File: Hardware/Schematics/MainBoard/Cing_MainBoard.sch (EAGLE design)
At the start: 178 parts, among them IC1 L293D, IC2 LM2576S, IC3 FT232RL, IC5 BME280, Q1 16mhz, Q2 BSS138, Q3 BSS138, Q4 BSS138, Q5 BSS138, Q6 NP2301AMR-G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

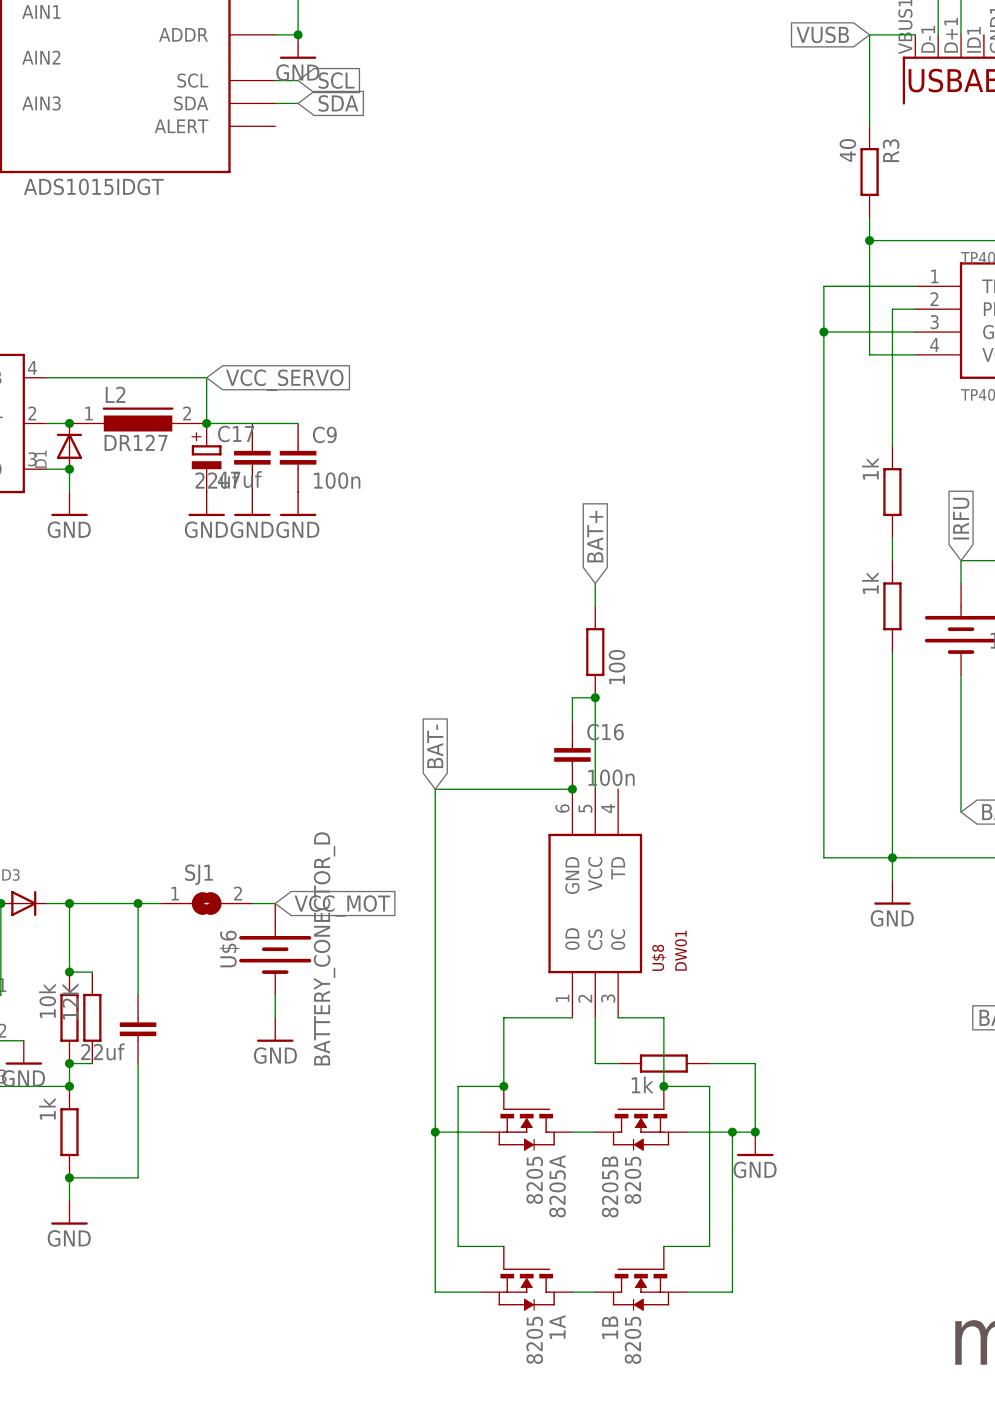
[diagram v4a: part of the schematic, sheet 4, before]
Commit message: adding more protection (motor fix)
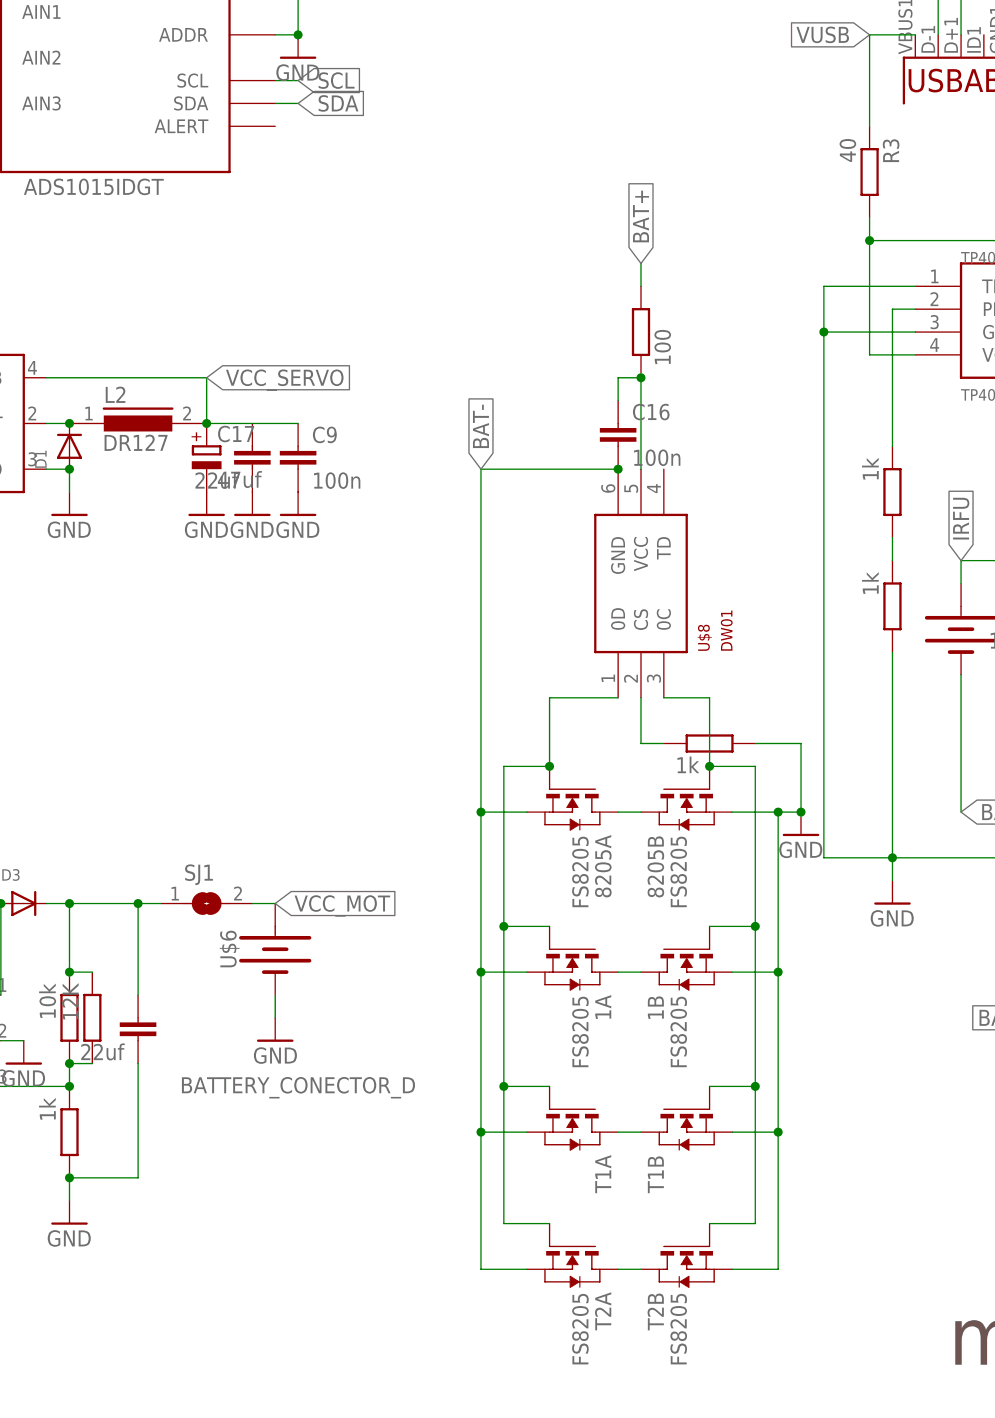
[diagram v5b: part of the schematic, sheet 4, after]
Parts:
- added T1, T2: FS8205, FS8205A:DMN3024LSD
- 1, 8205: value 8205 -> FS8205
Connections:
- new net N$67: T1A.D, T1B.D
- new net N$68: T2A.D, T2B.D
- net BAT-: now also T1A.S, T2A.S
- net GND: now also T1B.S, T2B.S
- net N$48: now also T1A.G, T2A.G
- net N$49: now also T1B.G, T2B.G
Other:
- moved on the sheet: 1A, 1B, 8205A, 8205B, C16, U$8

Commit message: adding CH330N
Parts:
- added C28, C29: 100n, rcl:C-EUC1206
- added U4: CH330N, Cing Library:CH330N
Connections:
- net +3V3: now also C28.1, C29.2, U4.V3, U4.VCC
- net D+: now also U4.USB_D+
- net D-: now also U4.USB_D-
- net GND: now also C28.2, C29.1, U1.USBID, U4.GND
- net RXD: now also U4.TXD
- net TXD: now also U4.RXD
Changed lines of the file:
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@@
 <part name="T1" library="FS8205A" deviceset="DMN3024LSD" device="" value="FS8205"/>
 <part name="T2" library="FS8205A" deviceset="DMN3024LSD" device="" value="FS8205"/>
+<part name="U4" library="Cing Library" library_urn="urn:adsk.eagle:library:10154637" deviceset="CH330N" device="" package3d_urn="urn:adsk.eagle:package:10906029/3"/>
+<part name="GND49" library="supply1" library_urn="urn:adsk.eagle:library:371" deviceset="GND" device=""/>
+<part name="C28" library="rcl" library_urn="urn:adsk.eagle:library:334" deviceset="C-EU" device="C1206" package3d_urn="urn:adsk.eagle:package:23618/2" value="100n"/>
+<part name="C29" library="rcl" library_urn="urn:adsk.eagle:library:334" deviceset="C-EU" device="C1206" package3d_urn="urn:adsk.eagle:package:23618/2" value="100n"/>
+<part name="GND61" library="supply1" library_urn="urn:adsk.eagle:library:371" deviceset="GND" device=""/>
+<part name="GND65" library="supply1" library_urn="urn:adsk.eagle:library:371" deviceset="GND" device=""/>
+<part name="+3V13" library="supply1" library_urn="urn:adsk.eagle:library:371" deviceset="+3V3" device=""/>
 </parts>
 <sheets>
@@
 <wire x1="175.26" y1="152.4" x2="170.18" y2="152.4" width="0.1524" layer="91"/>
 <pinref part="U1" gate="G$1" pin="GND"/>
+<pinref part="U1" gate="G$1" pin="USBID"/>
+<wire x1="170.18" y1="152.4" x2="167.64" y2="152.4" width="0.1524" layer="91"/>
+<junction x="170.18" y="152.4"/>
 </segment>
 <segment>
@@
 <attribute name="VALUE" x="200.66" y="132.08" size="1.778" layer="96"/>
 </instance>
-<instance part="R30" gate="G$1" x="175.26" y="83.82" smashed="yes" rot="MR90">
-<attribute name="VALUE" x="171.958" y="80.01" size="1.778" layer="96" rot="MR90"/>
-</instance>
-<instance part="R31" gate="G$1" x="180.34" y="83.82" smashed="yes" rot="MR90">
-<attribute name="VALUE" x="177.038" y="80.01" size="1.778" layer="96" rot="MR90"/>
-</instance>
-<instance part="+3V3" gate="G$1" x="177.8" y="99.06" smashed="yes">
-<attribute name="VALUE" x="175.26" y="93.98" size="1.778" layer="96" rot="R90"/>
+<instance part="R30" gate="G$1" x="187.96" y="106.68" smashed="yes" rot="MR90">
+<attribute name="VALUE" x="184.658" y="102.87" size="1.778" layer="96" rot="MR90"/>
+</instance>
+<instance part="R31" gate="G$1" x="193.04" y="106.68" smashed="yes" rot="MR90">
+<attribute name="VALUE" x="189.738" y="102.87" size="1.778" layer="96" rot="MR90"/>
+</instance>
+<instance part="+3V3" gate="G$1" x="190.5" y="121.92" smashed="yes">
+<attribute name="VALUE" x="187.96" y="116.84" size="1.778" layer="96" rot="R90"/>
 </instance>
 <instance part="+3V5" gate="G$1" x="210.82" y="152.4" smashed="yes">
@@
 <instance part="C22" gate="G$1" x="198.12" y="142.24" smashed="yes">
 <attribute name="VALUE" x="194.564" y="142.621" size="1.778" layer="96"/>
+</instance>
+<instance part="U4" gate="G$1" x="170.18" y="48.26" smashed="yes">
+<attribute name="NAME" x="175.26" y="58.42" size="2.1844" layer="95"/>
+<attribute name="VALUE" x="175.26" y="35.56" size="2.1844" layer="96"/>
+</instance>
+<instance part="GND49" gate="1" x="172.72" y="27.94" smashed="yes" rot="MR0">
+<attribute name="VALUE" x="175.26" y="25.4" size="1.778" layer="96" rot="MR0"/>
+</instance>
+<instance part="C28" gate="G$1" x="177.8" y="66.04" smashed="yes" rot="R90">
+<attribute name="NAME" x="177.419" y="67.564" size="1.778" layer="95" rot="R90"/>
+<attribute name="VALUE" x="182.499" y="67.564" size="1.778" layer="96" rot="R90"/>
+</instance>
+<instance part="C29" gate="G$1" x="165.1" y="66.04" smashed="yes" rot="R90">
+<attribute name="NAME" x="164.719" y="67.564" size="1.778" layer="95" rot="R90"/>
+<attribute name="VALUE" x="169.799" y="67.564" size="1.778" layer="96" rot="R90"/>
+</instance>
+<instance part="GND61" gate="1" x="182.88" y="60.96" smashed="yes" rot="MR0">
+<attribute name="VALUE" x="185.42" y="58.42" size="1.778" layer="96" rot="MR0"/>
+</instance>
+<instance part="GND65" gate="1" x="162.56" y="60.96" smashed="yes" rot="MR0">
+<attribute name="VALUE" x="165.1" y="58.42" size="1.778" layer="96" rot="MR0"/>
+</instance>
+<instance part="+3V13" gate="G$1" x="172.72" y="81.28" smashed="yes">
+<attribute name="VALUE" x="170.18" y="76.2" size="1.778" layer="96" rot="R90"/>
 </instance>
 </instances>
@@
 <pinref part="GND58" gate="1" pin="GND"/>
 </segment>
+<segment>
+<pinref part="U4" gate="G$1" pin="GND"/>
+<pinref part="GND49" gate="1" pin="GND"/>
+<wire x1="172.72" y1="30.48" x2="172.72" y2="33.02" width="0.1524" layer="91"/>
+</segment>
+<segment>
+<pinref part="C28" gate="G$1" pin="2"/>
+<pinref part="GND61" gate="1" pin="GND"/>
+<wire x1="182.88" y1="66.04" x2="182.88" y2="63.5" width="0.1524" layer="91"/>
+</segment>
+<segment>
+<pinref part="C29" gate="G$1" pin="1"/>
+<pinref part="GND65" gate="1" pin="GND"/>
+<wire x1="162.56" y1="66.04" x2="162.56" y2="63.5" width="0.1524" layer="91"/>
+</segment>
 </net>
 <net name="N$20" class="0">
@@
 <pinref part="IC3" gate="G$1" pin="USBDM"/>
 </segment>
+<segment>
+<pinref part="U4" gate="G$1" pin="USB_D-"/>
+<wire x1="190.5" y1="48.26" x2="193.04" y2="48.26" width="0.1524" layer="91"/>
+<label x="193.04" y="48.26" size="1.778" layer="95" xref="yes"/>
+</segment>
 </net>
 <net name="D+" class="0">
@@
 <label x="106.68" y="137.16" size="1.778" layer="95" rot="R180" xref="yes"/>
 <pinref part="IC3" gate="G$1" pin="USBDP"/>
+</segment>
+<segment>
+<pinref part="U4" gate="G$1" pin="USB_D+"/>
+<wire x1="190.5" y1="43.18" x2="193.04" y2="43.18" width="0.1524" layer="91"/>
+<label x="193.04" y="43.18" size="1.778" layer="95" xref="yes"/>
 </segment>
 </net>
@@
 <wire x1="157.48" y1="154.94" x2="157.48" y2="144.78" width="0.1524" layer="91"/>
 </segment>
+<segment>
+<pinref part="U4" gate="G$1" pin="RXD"/>
+<wire x1="154.94" y1="53.34" x2="152.4" y2="53.34" width="0.1524" layer="91"/>
+<label x="152.4" y="53.34" size="1.778" layer="95" rot="R180" xref="yes"/>
+</segment>
 </net>
 <net name="RXD" class="0">
@@
 <wire x1="152.4" y1="154.94" x2="152.4" y2="147.32" width="0.1524" layer="91"/>
 </segment>
+<segment>
+<pinref part="U4" gate="G$1" pin="TXD"/>
+<wire x1="154.94" y1="43.18" x2="152.4" y2="43.18" width="0.1524" layer="91"/>
+<label x="152.4" y="43.18" size="1.778" layer="95" rot="R180" xref="yes"/>
+</segment>
 </net>
 <net name="SCL" class="0">
@@
 <segment>
 <pinref part="R30" gate="G$1" pin="1"/>
-<wire x1="175.26" y1="78.74" x2="170.18" y2="78.74" width="0.1524" layer="91"/>
-<label x="170.18" y="78.74" size="1.778" layer="95" rot="R180" xref="yes"/>
+<wire x1="187.96" y1="101.6" x2="182.88" y2="101.6" width="0.1524" layer="91"/>
+<label x="182.88" y="101.6" size="1.778" layer="95" rot="R180" xref="yes"/>
 </segment>
 <segment>
@@
 <segment>
 <pinref part="R31" gate="G$1" pin="1"/>
-<wire x1="180.34" y1="78.74" x2="182.88" y2="78.74" width="0.1524" layer="91"/>
-<label x="182.88" y="78.74" size="1.778" layer="95" xref="yes"/>
+<wire x1="193.04" y1="101.6" x2="195.58" y2="101.6" width="0.1524" layer="91"/>
+<label x="195.58" y="101.6" size="1.778" layer="95" xref="yes"/>
 </segment>
 <segment>
@@
 <pinref part="R30" gate="G$1" pin="2"/>
 <pinref part="R31" gate="G$1" pin="2"/>
-<wire x1="180.34" y1="88.9" x2="177.8" y2="88.9" width="0.1524" layer="91"/>
+<wire x1="193.04" y1="111.76" x2="190.5" y2="111.76" width="0.1524" layer="91"/>
 <pinref part="+3V3" gate="G$1" pin="+3V3"/>
-<wire x1="177.8" y1="96.52" x2="177.8" y2="88.9" width="0.1524" layer="91"/>
-<junction x="177.8" y="88.9"/>
-<wire x1="177.8" y1="88.9" x2="175.26" y2="88.9" width="0.1524" layer="91"/>
+<wire x1="190.5" y1="119.38" x2="190.5" y2="111.76" width="0.1524" layer="91"/>
+<junction x="190.5" y="111.76"/>
+<wire x1="190.5" y1="111.76" x2="187.96" y2="111.76" width="0.1524" layer="91"/>
 </segment>
 <segment>
@@
 <pinref part="+3V38" gate="G$1" pin="+3V3"/>
 </segment>
-</net>
+<segment>
+<pinref part="U4" gate="G$1" pin="VCC"/>
+<pinref part="C28" gate="G$1" pin="1"/>
+<wire x1="175.26" y1="66.04" x2="175.26" y2="63.5" width="0.1524" layer="91"/>
+<pinref part="U4" gate="G$1" pin="V3"/>
+<pinref part="C29" gate="G$1" pin="2"/>
+<wire x1="170.18" y1="66.04" x2="170.18" y2="63.5" width="0.1524" layer="91"/>
+<wire x1="175.26" y1="66.04" x2="172.72" y2="66.04" width="0.1524" layer="91"/>
+<junction x="175.26" y="66.04"/>
+<junction x="170.18" y="66.04"/>
+<pinref part="+3V13" gate="G$1" pin="+3V3"/>
+<wire x1="172.72" y1="66.04" x2="170.18" y2="66.04" width="0.1524" layer="91"/>
+<wire x1="172.72" y1="66.04" x2="172.72" y2="78.74" width="0.1524" layer="91"/>
+<junction x="172.72" y="66.04"/>
+</segment>
+</net>

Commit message: commit
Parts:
- added C30, C31: 100n, rcl:C-EUC1206
- added IC4: BMP280, bosch-bmp280:BMP280
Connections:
- net +3V3: now also C30.2, C31.2, IC4.CSB, IC4.SDO, IC4.VDD, IC4.VDDIO
- net GND: now also C30.1, C31.1, IC4.GND
- net SCL: now also IC4.SCK
- net SDA: now also IC4.SDI
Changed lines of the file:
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@@
 <part name="GND65" library="supply1" library_urn="urn:adsk.eagle:library:371" deviceset="GND" device=""/>
 <part name="+3V13" library="supply1" library_urn="urn:adsk.eagle:library:371" deviceset="+3V3" device=""/>
+<part name="FRAME7" library="frames" library_urn="urn:adsk.eagle:library:229" deviceset="A4L-LOC" device=""/>
+<part name="IC4" library="bosch-bmp280" deviceset="BMP280" device=""/>
+<part name="+3V14" library="supply1" library_urn="urn:adsk.eagle:library:371" deviceset="+3V3" device=""/>
+<part name="+3V15" library="supply1" library_urn="urn:adsk.eagle:library:371" deviceset="+3V3" device=""/>
+<part name="GND71" library="supply1" library_urn="urn:adsk.eagle:library:371" deviceset="GND" device=""/>
+<part name="+3V16" library="supply1" library_urn="urn:adsk.eagle:library:371" deviceset="+3V3" device=""/>
+<part name="+3V19" library="supply1" library_urn="urn:adsk.eagle:library:371" deviceset="+3V3" device=""/>
+<part name="C30" library="rcl" library_urn="urn:adsk.eagle:library:334" deviceset="C-EU" device="C1206" package3d_urn="urn:adsk.eagle:package:23618/2" value="100n"/>
+<part name="+3V24" library="supply1" library_urn="urn:adsk.eagle:library:371" deviceset="+3V3" device=""/>
+<part name="GND72" library="supply1" library_urn="urn:adsk.eagle:library:371" deviceset="GND" device=""/>
+<part name="C31" library="rcl" library_urn="urn:adsk.eagle:library:334" deviceset="C-EU" device="C1206" package3d_urn="urn:adsk.eagle:package:23618/2" value="100n"/>
+<part name="+3V25" library="supply1" library_urn="urn:adsk.eagle:library:371" deviceset="+3V3" device=""/>
+<part name="GND73" library="supply1" library_urn="urn:adsk.eagle:library:371" deviceset="GND" device=""/>
 </parts>
 <sheets>
@@
 <attribute name="VALUE" x="170.18" y="76.2" size="1.778" layer="96" rot="R90"/>
 </instance>
+<instance part="IC4" gate="G$1" x="223.52" y="40.64" smashed="yes">
+<attribute name="NAME" x="213.614" y="49.022" size="1.778" layer="95" font="vector"/>
+<attribute name="VALUE" x="213.36" y="30.48" size="1.778" layer="96" font="vector"/>
+</instance>
+<instance part="+3V14" gate="G$1" x="208.28" y="48.26" smashed="yes">
+<attribute name="VALUE" x="208.28" y="48.26" size="1.778" layer="96" rot="R90"/>
+</instance>
+<instance part="+3V15" gate="G$1" x="238.76" y="48.26" smashed="yes">
+<attribute name="VALUE" x="236.22" y="43.18" size="1.778" layer="96" rot="R90"/>
+</instance>
+<instance part="GND71" gate="1" x="208.28" y="33.02" smashed="yes" rot="MR0">
+<attribute name="VALUE" x="210.82" y="30.48" size="1.778" layer="96" rot="MR0"/>
+</instance>
+<instance part="+3V16" gate="G$1" x="208.28" y="43.18" smashed="yes">
+<attribute name="VALUE" x="208.28" y="43.18" size="1.778" layer="96" rot="R90"/>
+</instance>
+<instance part="+3V19" gate="G$1" x="241.3" y="35.56" smashed="yes" rot="R270">
+<attribute name="VALUE" x="241.3" y="33.02" size="1.778" layer="96"/>
+</instance>
+<instance part="C30" gate="G$1" x="243.84" y="53.34" smashed="yes" rot="R180">
+<attribute name="NAME" x="242.316" y="52.959" size="1.778" layer="95" rot="R180"/>
+<attribute name="VALUE" x="242.316" y="58.039" size="1.778" layer="96" rot="R180"/>
+</instance>
+<instance part="+3V24" gate="G$1" x="243.84" y="60.96" smashed="yes">
+<attribute name="VALUE" x="241.3" y="55.88" size="1.778" layer="96" rot="R90"/>
+</instance>
+<instance part="GND72" gate="1" x="243.84" y="48.26" smashed="yes" rot="MR0">
+<attribute name="VALUE" x="246.38" y="45.72" size="1.778" layer="96" rot="MR0"/>
+</instance>
+<instance part="C31" gate="G$1" x="251.46" y="53.34" smashed="yes" rot="R180">
+<attribute name="NAME" x="249.936" y="52.959" size="1.778" layer="95" rot="R180"/>
+<attribute name="VALUE" x="249.936" y="58.039" size="1.778" layer="96" rot="R180"/>
+</instance>
+<instance part="+3V25" gate="G$1" x="251.46" y="60.96" smashed="yes">
+<attribute name="VALUE" x="248.92" y="55.88" size="1.778" layer="96" rot="R90"/>
+</instance>
+<instance part="GND73" gate="1" x="251.46" y="48.26" smashed="yes" rot="MR0">
+<attribute name="VALUE" x="254" y="45.72" size="1.778" layer="96" rot="MR0"/>
+</instance>
 </instances>
 <busses>
@@
 <wire x1="162.56" y1="66.04" x2="162.56" y2="63.5" width="0.1524" layer="91"/>
 </segment>
+<segment>
+<pinref part="IC4" gate="G$1" pin="GND"/>
+<pinref part="GND71" gate="1" pin="GND"/>
+</segment>
+<segment>
+<pinref part="C30" gate="G$1" pin="1"/>
+<pinref part="GND72" gate="1" pin="GND"/>
+</segment>
+<segment>
+<pinref part="C31" gate="G$1" pin="1"/>
+<pinref part="GND73" gate="1" pin="GND"/>
+</segment>
 </net>
 <net name="N$20" class="0">
@@
 <label x="231.14" y="68.58" size="1.778" layer="95" xref="yes"/>
 </segment>
+<segment>
+<pinref part="IC4" gate="G$1" pin="SCK"/>
+<wire x1="238.76" y1="40.64" x2="241.3" y2="40.64" width="0.1524" layer="91"/>
+<label x="241.3" y="40.64" size="1.778" layer="95" xref="yes"/>
+</segment>
 </net>
 <net name="SDA" class="0">
@@
 <label x="231.14" y="66.04" size="1.778" layer="95" xref="yes"/>
 </segment>
+<segment>
+<pinref part="IC4" gate="G$1" pin="SDI"/>
+<wire x1="238.76" y1="38.1" x2="241.3" y2="38.1" width="0.1524" layer="91"/>
+<label x="241.3" y="38.1" size="1.778" layer="95" xref="yes"/>
+</segment>
 </net>
 <net name="+3V3" class="0">
@@
 <junction x="172.72" y="66.04"/>
 </segment>
+<segment>
+<pinref part="IC4" gate="G$1" pin="VDD"/>
+<pinref part="+3V14" gate="G$1" pin="+3V3"/>
+</segment>
+<segment>
+<pinref part="IC4" gate="G$1" pin="VDDIO"/>
+<pinref part="+3V15" gate="G$1" pin="+3V3"/>
+</segment>
+<segment>
+<pinref part="IC4" gate="G$1" pin="CSB"/>
+<pinref part="+3V16" gate="G$1" pin="+3V3"/>
+</segment>
+<segment>
+<pinref part="IC4" gate="G$1" pin="SDO"/>
+<pinref part="+3V19" gate="G$1" pin="+3V3"/>
+</segment>
+<segment>
+<pinref part="C30" gate="G$1" pin="2"/>
+<pinref part="+3V24" gate="G$1" pin="+3V3"/>
+</segment>
+<segment>
+<pinref part="C31" gate="G$1" pin="2"/>
+<pinref part="+3V25" gate="G$1" pin="+3V3"/>
+</segment>
 </net>
 <net name="SCK" class="0">
@@
 </nets>
 </sheet>
+<sheet>
+<description>Board sensors and outputs</description>
+<plain>
+</plain>
+<instances>
+<instance part="FRAME7" gate="G$1" x="0" y="0" smashed="yes">
+<attribute name="LAST_DATE_TIME" x="217.17" y="10.16" size="2.286" layer="94"/>
+<attribute name="SHEET" x="230.505" y="5.08" size="2.54" layer="94"/>
+</instance>
+</instances>
+<busses>
+</busses>
+<nets>
+</nets>
+</sheet>

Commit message: adding minor fixes
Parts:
- R22, R6: value 100 -> R100
- R41: device rcl:R-EU_R2512 -> rcl:R-EU_R1206
